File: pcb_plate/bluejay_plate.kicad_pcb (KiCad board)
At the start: 2 copper layers, 147.1 x 138.9 mm, 33 parts

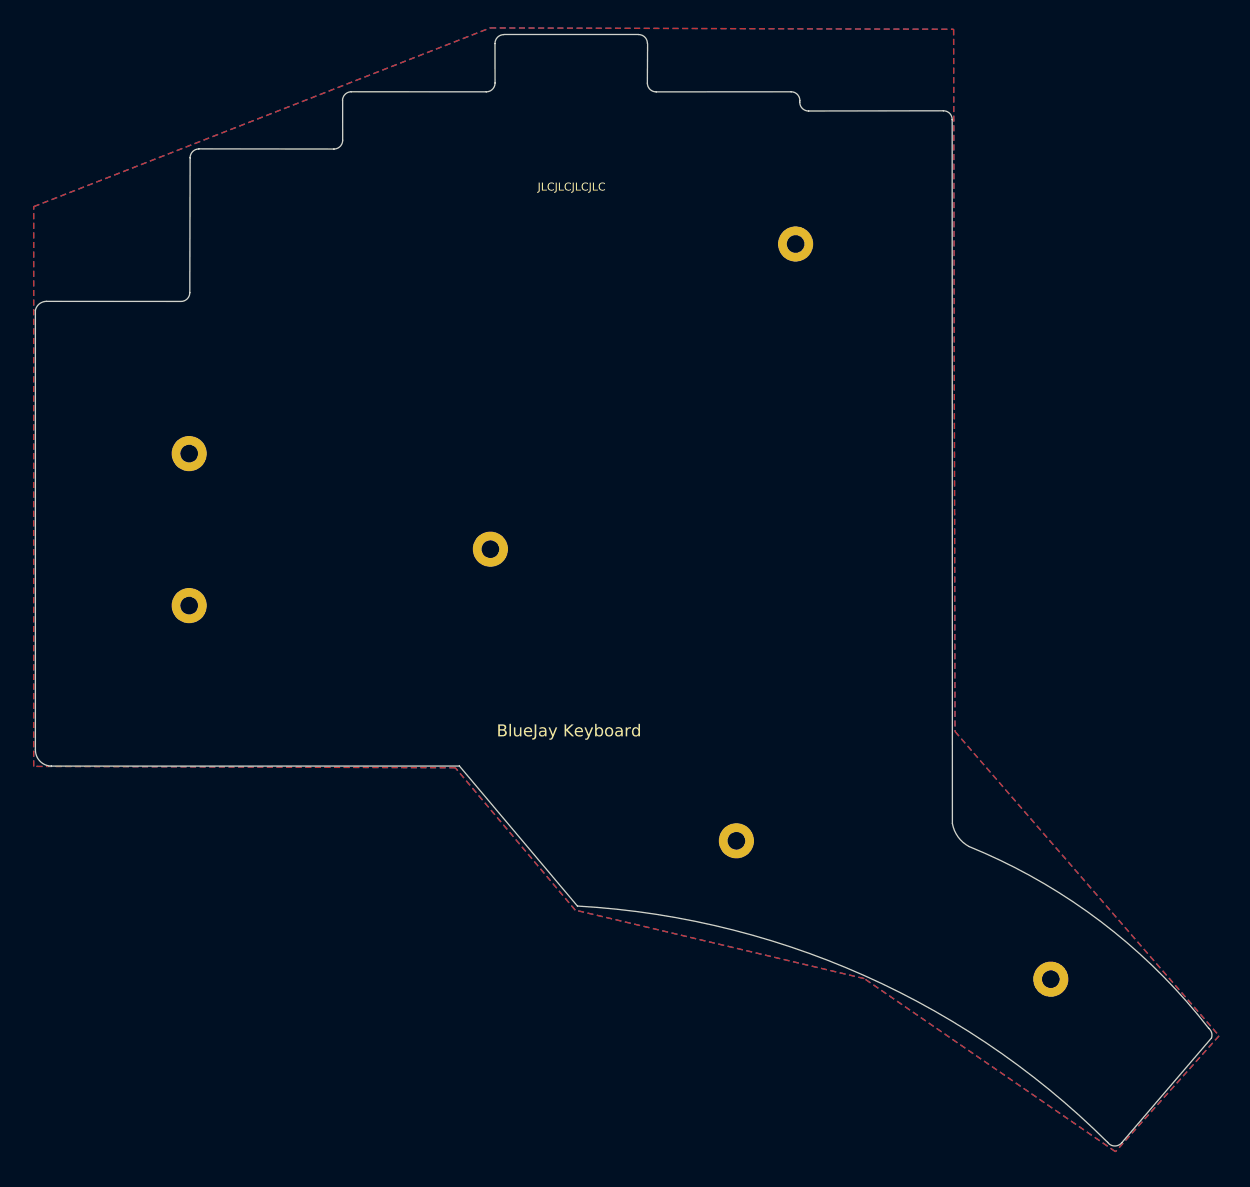
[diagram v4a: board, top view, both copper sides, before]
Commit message: Round edges of PCB
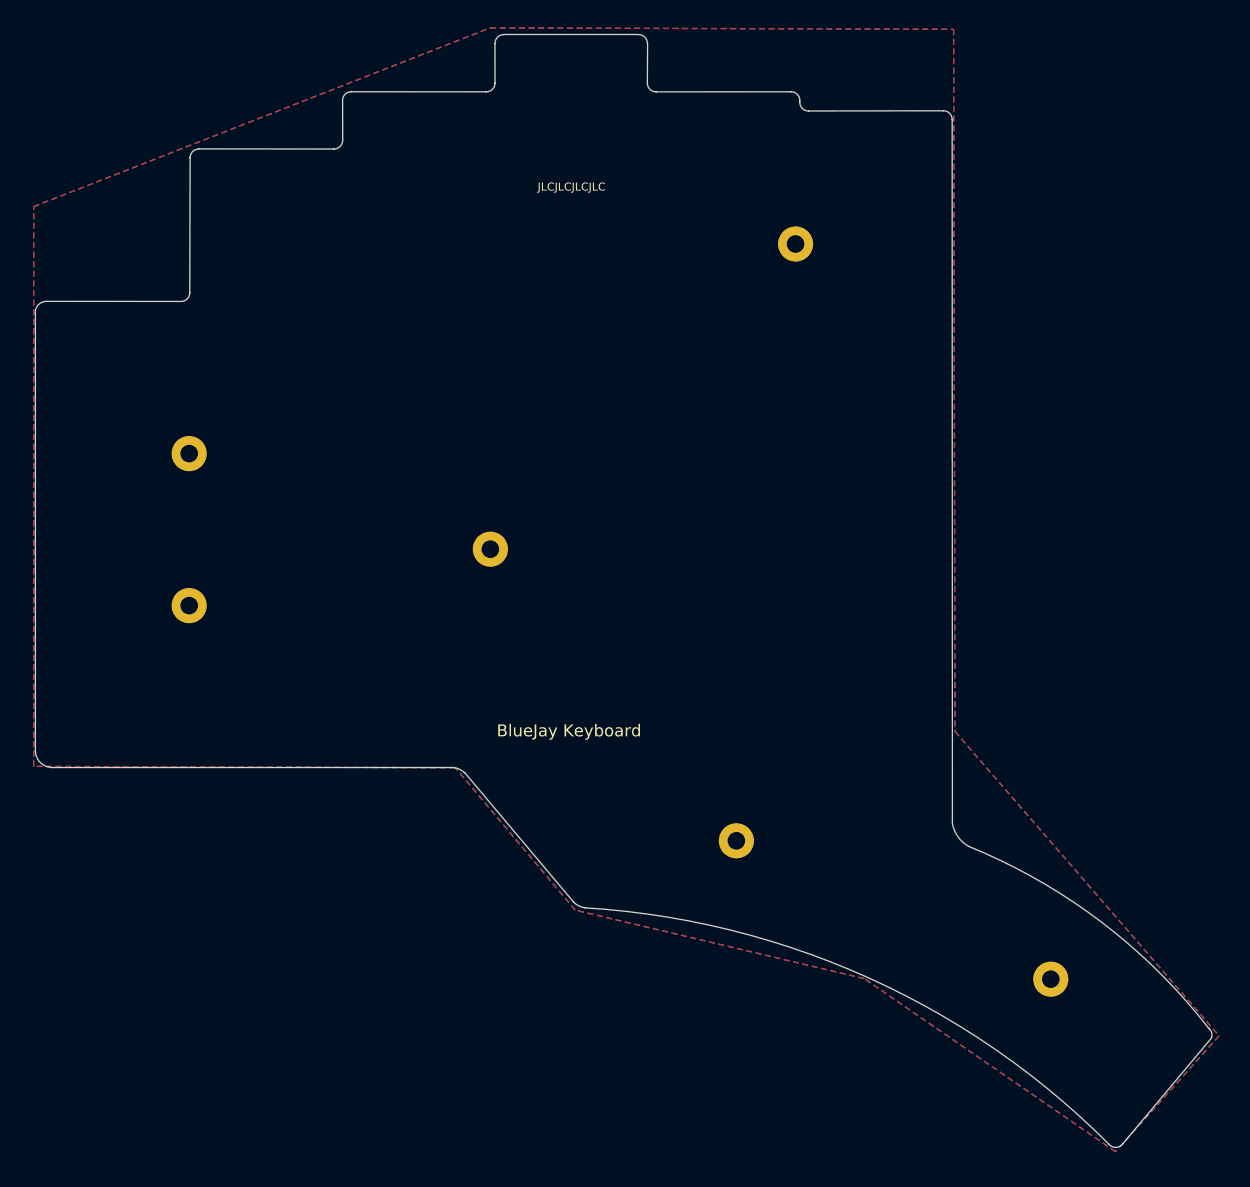
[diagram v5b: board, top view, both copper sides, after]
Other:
- board size 147.1 x 138.9 mm -> 147.1 x 139.1 mm
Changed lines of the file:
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@@
   (gr_line (start 10.630746 -45.224889) (end 27.48 -45.25) (layer "Edge.Cuts") (width 0.1))
   (gr_line (start -84.655111 -21.429254) (end -67.814889 -21.420746) (layer "Edge.Cuts") (width 0.1))
-  (gr_line (start 60.9812 70.6563) (end 49.7812 83.7263) (layer "Edge.Cuts") (width 0.1))
+  (gr_line (start 60.987489 70.653008) (end 49.88 83.9) (layer "Edge.Cuts") (width 0.1))
   (gr_line (start -47.62 -46.519254) (end -47.614889 -41.580746) (layer "Edge.Cuts") (width 0.1))
   (gr_arc (start -10.620197 -54.774034) (mid -9.84 -54.45) (end -9.530197 -53.664034) (layer "Edge.Cuts") (width 0.1))
@@
   (gr_line (start -10.620197 -54.79) (end -27.485111 -54.79) (layer "Edge.Cuts") (width 0.1))
   (gr_line (start -65.595111 -40.49) (end -48.704889 -40.470746) (layer "Edge.Cuts") (width 0.1))
+  (gr_arc (start -17.32 54.38) (mid -18.079496 54.13977) (end -18.73 53.68) (layer "Edge.Cuts") (width 0.1))
   (gr_line (start -46.56 -47.629254) (end -29.66 -47.62) (layer "Edge.Cuts") (width 0.1))
   (gr_line (start 9.52845 -46.515422) (end 9.520746 -46.314889) (layer "Edge.Cuts") (width 0.1))
   (gr_line (start -9.5 -53.664034) (end -9.529254 -48.704889) (layer "Edge.Cuts") (width 0.1))
-  (gr_arc (start -18.2688 54.1563) (mid 17.583107 62.841492) (end 48.0112 83.6963) (layer "Edge.Cuts") (width 0.1))
+  (gr_arc (start -17.32 54.38) (mid 18.101214 63.120674) (end 48.11 83.87) (layer "Edge.Cuts") (width 0.1))
   (gr_line (start 28.57 -44.15) (end 28.6 43.85) (layer "Edge.Cuts") (width 0.1))
   (gr_arc (start 60.64 69.44) (mid 61.003391 69.992176) (end 60.987489 70.653008) (layer "Edge.Cuts") (width 0.1))
   (gr_arc (start 27.48 -45.25) (mid 28.26155 -44.924578) (end 28.57 -44.14) (layer "Edge.Cuts") (width 0.1))
-  (gr_arc (start -84.02552 36.663017) (mid -85.443204 36.061839) (end -86.025519 34.6363) (layer "Edge.Cuts") (width 0.1))
-  (gr_line (start -86.024883 -20.32) (end -86.025519 34.6363) (layer "Edge.Cuts") (width 0.1))
+  (gr_arc (start -83.93 36.84) (mid -85.382325 36.242623) (end -86.025519 34.81) (layer "Edge.Cuts") (width 0.1))
+  (gr_line (start -86.024883 -20.32) (end -86.025519 34.81) (layer "Edge.Cuts") (width 0.1))
   (gr_line (start -66.685111 -39.4) (end -66.724889 -22.52) (layer "Edge.Cuts") (width 0.1))
-  (gr_line (start -84.02552 36.663017) (end -33.0188 36.6563) (layer "Edge.Cuts") (width 0.1))
+  (gr_line (start -83.93 36.84) (end -33.72 36.84) (layer "Edge.Cuts") (width 0.1))
   (gr_arc (start 10.630746 -45.224889) (mid 9.85 -45.54) (end 9.520746 -46.314889) (layer "Edge.Cuts") (width 0.1))
   (gr_arc (start -8.419254 -47.614889) (mid -9.2 -47.93) (end -9.529254 -48.704889) (layer "Edge.Cuts") (width 0.1))
   (gr_arc (start -47.614889 -41.580746) (mid -47.93 -40.8) (end -48.704889 -40.470746) (layer "Edge.Cuts") (width 0.1))
-  (gr_line (start -33.0188 36.6563) (end -18.2688 54.1563) (layer "Edge.Cuts") (width 0.1))
+  (gr_line (start -32.31 37.54) (end -18.73 53.68) (layer "Edge.Cuts") (width 0.1))
   (gr_arc (start 30.69 46.72) (mid 47.162468 56.106012) (end 60.64 69.44) (layer "Edge.Cuts") (width 0.1))
   (gr_line (start -8.419254 -47.614889) (end 8.45 -47.625422) (layer "Edge.Cuts") (width 0.1))
+  (gr_arc (start -33.72 36.84) (mid -32.960504 37.08023) (end -32.31 37.54) (layer "Edge.Cuts") (width 0.1))
   (gr_arc (start -66.724889 -22.530746) (mid -67.04 -21.75) (end -67.814889 -21.420746) (layer "Edge.Cuts") (width 0.1))
   (gr_arc (start -28.57 -48.73) (mid -28.885111 -47.949254) (end -29.66 -47.62) (layer "Edge.Cuts") (width 0.1))
   (gr_arc (start 30.69 46.72) (mid 29.316945 45.522681) (end 28.6 43.85) (layer "Edge.Cuts") (width 0.1))
   (gr_arc (start -28.575111 -53.659254) (mid -28.26 -54.44) (end -27.485111 -54.769254) (layer "Edge.Cuts") (width 0.1))
-  (gr_arc (start 49.7812 83.7263) (mid 48.888799 84.147698) (end 48.0112 83.6963) (layer "Edge.Cuts") (width 0.1))
+  (gr_arc (start 49.88 83.9) (mid 48.987603 84.321434) (end 48.11 83.87) (layer "Edge.Cuts") (width 0.1))
   (gr_arc (start -66.685111 -39.369254) (mid -66.37 -40.15) (end -65.595111 -40.479254) (layer "Edge.Cuts") (width 0.1))
   (gr_arc (start 8.43845 -47.625422) (mid 9.218647 -47.301388) (end 9.52845 -46.515422) (layer "Edge.Cuts") (width 0.1))

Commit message: Fine tuning of edge cut for plate
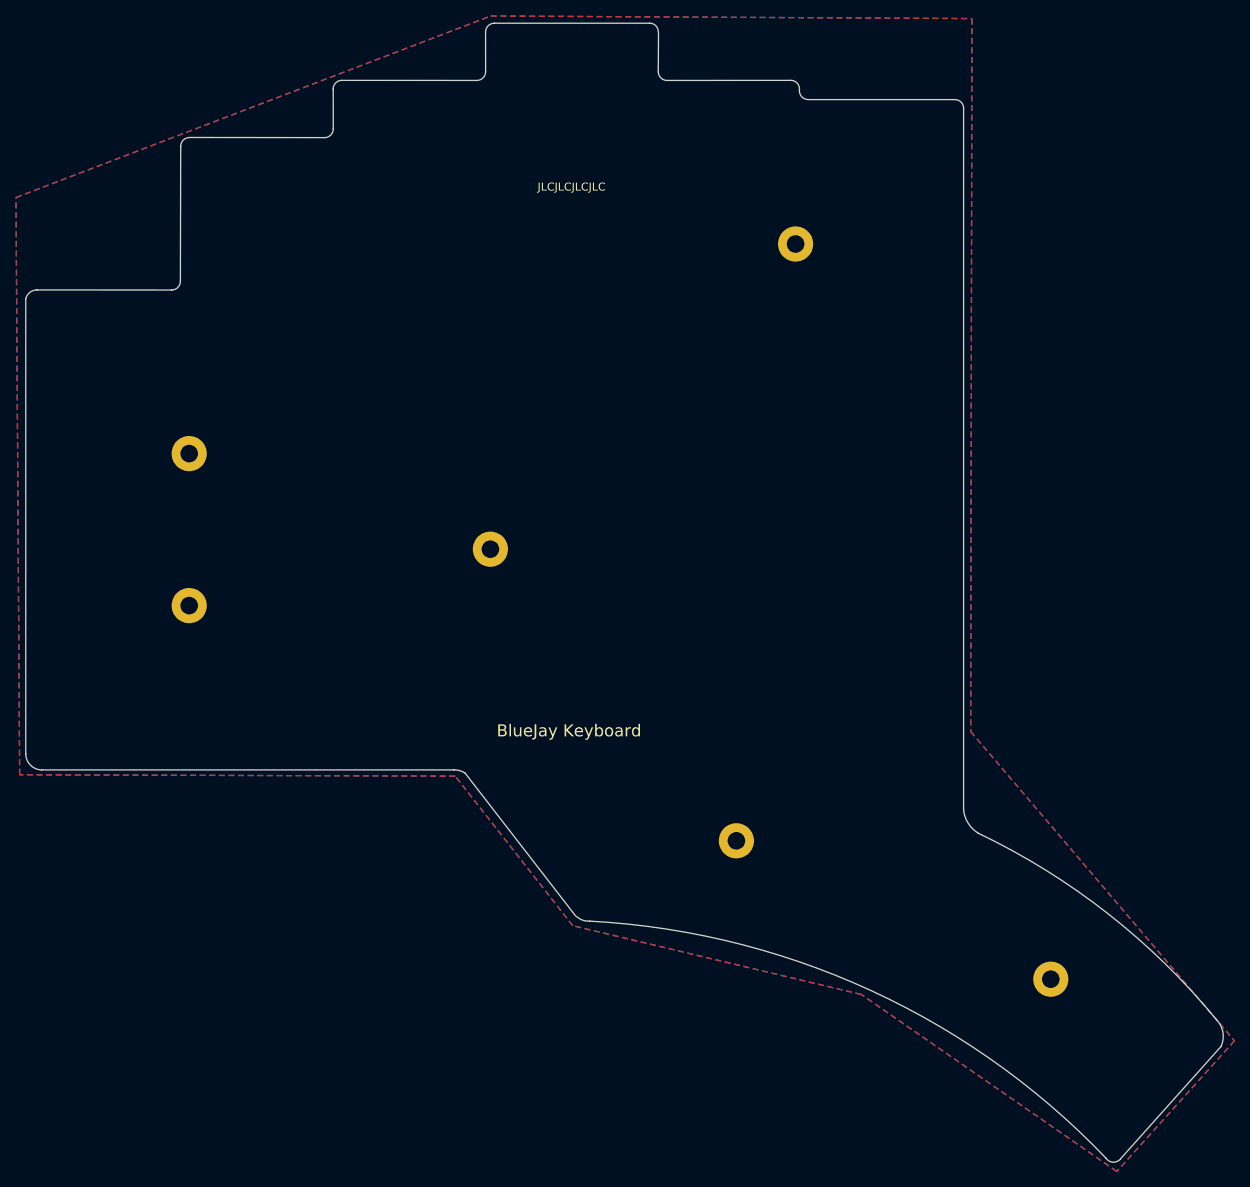
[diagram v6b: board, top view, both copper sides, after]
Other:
- board size 147.1 x 139.1 mm -> 149.7 x 142.4 mm
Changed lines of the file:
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@@
   (gr_line locked (start 26.028999 -42.674998) (end 26.028999 -42.674998) (layer "Eco1.User") (width 0.188976))
   (gr_line locked (start -16.546013 52.286989) (end -16.546013 38.286989) (layer "Eco1.User") (width 0.188976))
-  (gr_arc (start -47.635111 -46.519254) (mid -47.32 -47.3) (end -46.545111 -47.629254) (layer "Edge.Cuts") (width 0.1))
-  (gr_arc (start -86.024883 -20.32) (mid -85.533559 -21.113649) (end -84.655111 -21.429254) (layer "Edge.Cuts") (width 0.1))
-  (gr_line (start 10.630746 -45.224889) (end 27.48 -45.25) (layer "Edge.Cuts") (width 0.1))
-  (gr_line (start -84.655111 -21.429254) (end -67.814889 -21.420746) (layer "Edge.Cuts") (width 0.1))
-  (gr_line (start 60.987489 70.653008) (end 49.88 83.9) (layer "Edge.Cuts") (width 0.1))
-  (gr_line (start -47.62 -46.519254) (end -47.614889 -41.580746) (layer "Edge.Cuts") (width 0.1))
-  (gr_arc (start -10.620197 -54.774034) (mid -9.84 -54.45) (end -9.530197 -53.664034) (layer "Edge.Cuts") (width 0.1))
-  (gr_line (start -28.575111 -53.659254) (end -28.57 -48.73) (layer "Edge.Cuts") (width 0.1))
-  (gr_line (start -10.620197 -54.79) (end -27.485111 -54.79) (layer "Edge.Cuts") (width 0.1))
-  (gr_line (start -65.595111 -40.49) (end -48.704889 -40.470746) (layer "Edge.Cuts") (width 0.1))
-  (gr_arc (start -17.32 54.38) (mid -18.079496 54.13977) (end -18.73 53.68) (layer "Edge.Cuts") (width 0.1))
-  (gr_line (start -46.56 -47.629254) (end -29.66 -47.62) (layer "Edge.Cuts") (width 0.1))
-  (gr_line (start 9.52845 -46.515422) (end 9.520746 -46.314889) (layer "Edge.Cuts") (width 0.1))
-  (gr_line (start -9.5 -53.664034) (end -9.529254 -48.704889) (layer "Edge.Cuts") (width 0.1))
-  (gr_arc (start -17.32 54.38) (mid 18.101214 63.120674) (end 48.11 83.87) (layer "Edge.Cuts") (width 0.1))
-  (gr_line (start 28.57 -44.15) (end 28.6 43.85) (layer "Edge.Cuts") (width 0.1))
-  (gr_arc (start 60.64 69.44) (mid 61.003391 69.992176) (end 60.987489 70.653008) (layer "Edge.Cuts") (width 0.1))
-  (gr_arc (start 27.48 -45.25) (mid 28.26155 -44.924578) (end 28.57 -44.14) (layer "Edge.Cuts") (width 0.1))
-  (gr_arc (start -83.93 36.84) (mid -85.382325 36.242623) (end -86.025519 34.81) (layer "Edge.Cuts") (width 0.1))
-  (gr_line (start -86.024883 -20.32) (end -86.025519 34.81) (layer "Edge.Cuts") (width 0.1))
-  (gr_line (start -66.685111 -39.4) (end -66.724889 -22.52) (layer "Edge.Cuts") (width 0.1))
-  (gr_line (start -83.93 36.84) (end -33.72 36.84) (layer "Edge.Cuts") (width 0.1))
-  (gr_arc (start 10.630746 -45.224889) (mid 9.85 -45.54) (end 9.520746 -46.314889) (layer "Edge.Cuts") (width 0.1))
-  (gr_arc (start -8.419254 -47.614889) (mid -9.2 -47.93) (end -9.529254 -48.704889) (layer "Edge.Cuts") (width 0.1))
-  (gr_arc (start -47.614889 -41.580746) (mid -47.93 -40.8) (end -48.704889 -40.470746) (layer "Edge.Cuts") (width 0.1))
-  (gr_line (start -32.31 37.54) (end -18.73 53.68) (layer "Edge.Cuts") (width 0.1))
-  (gr_arc (start 30.69 46.72) (mid 47.162468 56.106012) (end 60.64 69.44) (layer "Edge.Cuts") (width 0.1))
-  (gr_line (start -8.419254 -47.614889) (end 8.45 -47.625422) (layer "Edge.Cuts") (width 0.1))
-  (gr_arc (start -33.72 36.84) (mid -32.960504 37.08023) (end -32.31 37.54) (layer "Edge.Cuts") (width 0.1))
-  (gr_arc (start -66.724889 -22.530746) (mid -67.04 -21.75) (end -67.814889 -21.420746) (layer "Edge.Cuts") (width 0.1))
-  (gr_arc (start -28.57 -48.73) (mid -28.885111 -47.949254) (end -29.66 -47.62) (layer "Edge.Cuts") (width 0.1))
-  (gr_arc (start 30.69 46.72) (mid 29.316945 45.522681) (end 28.6 43.85) (layer "Edge.Cuts") (width 0.1))
-  (gr_arc (start -28.575111 -53.659254) (mid -28.26 -54.44) (end -27.485111 -54.769254) (layer "Edge.Cuts") (width 0.1))
-  (gr_arc (start 49.88 83.9) (mid 48.987603 84.321434) (end 48.11 83.87) (layer "Edge.Cuts") (width 0.1))
-  (gr_arc (start -66.685111 -39.369254) (mid -66.37 -40.15) (end -65.595111 -40.479254) (layer "Edge.Cuts") (width 0.1))
-  (gr_arc (start 8.43845 -47.625422) (mid 9.218647 -47.301388) (end 9.52845 -46.515422) (layer "Edge.Cuts") (width 0.1))
+  (gr_arc (start -48.811552 -47.945605) (mid -48.496441 -48.726351) (end -47.721552 -49.055605) (layer "Edge.Cuts") (width 0.1))
+  (gr_arc (start -87.23 -21.74) (mid -86.725569 -22.541982) (end -85.831552 -22.855605) (layer "Edge.Cuts") (width 0.1))
+  (gr_line (start 10.630746 -46.65) (end 28.91 -46.65) (layer "Edge.Cuts") (width 0.1))
+  (gr_line (start -85.831552 -22.855605) (end -68.99133 -22.847097) (layer "Edge.Cuts") (width 0.1))
+  (gr_line (start 62.17 71.72) (end 49.62 85.75) (layer "Edge.Cuts") (width 0.1))
+  (gr_line (start -48.796441 -47.945605) (end -48.79133 -43.007097) (layer "Edge.Cuts") (width 0.1))
+  (gr_arc (start -9.25557 -56.203879) (mid -8.47537 -55.879841) (end -8.16557 -55.093879) (layer "Edge.Cuts") (width 0.1))
+  (gr_line (start -29.751552 -55.085605) (end -29.746441 -50.156351) (layer "Edge.Cuts") (width 0.1))
+  (gr_line (start -9.26 -56.2) (end -28.66 -56.2) (layer "Edge.Cuts") (width 0.1))
+  (gr_line (start -66.771552 -41.916351) (end -49.88133 -41.897097) (layer "Edge.Cuts") (width 0.1))
+  (gr_arc (start -16.74 56.04) (mid -17.619397 55.917949) (end -18.38 55.46) (layer "Edge.Cuts") (width 0.1))
+  (gr_line (start -47.736441 -49.055605) (end -30.836441 -49.046351) (layer "Edge.Cuts") (width 0.1))
+  (gr_line (start 9.483077 -47.945267) (end 9.475373 -47.744734) (layer "Edge.Cuts") (width 0.1))
+  (gr_line (start -8.135373 -55.093879) (end -8.164627 -50.134734) (layer "Edge.Cuts") (width 0.1))
+  (gr_arc (start -16.74 56.04) (mid 18.380681 64.696706) (end 47.83 85.7) (layer "Edge.Cuts") (width 0.1))
+  (gr_line (start 30 -45.54) (end 30 42.15) (layer "Edge.Cuts") (width 0.1))
+  (gr_arc (start 61.62 68.37) (mid 62.419111 69.958952) (end 62.17 71.72) (layer "Edge.Cuts") (width 0.1))
+  (gr_arc (start 28.91 -46.65) (mid 29.690197 -46.325966) (end 30 -45.54) (layer "Edge.Cuts") (width 0.1))
+  (gr_arc (start -85.23 37.14) (mid -86.648353 36.53717) (end -87.23 35.11) (layer "Edge.Cuts") (width 0.1))
+  (gr_line (start -87.23 -21.74) (end -87.23 35.11) (layer "Edge.Cuts") (width 0.1))
+  (gr_line (start -67.861552 -40.826351) (end -67.90133 -23.946351) (layer "Edge.Cuts") (width 0.1))
+  (gr_line (start -85.23 37.14) (end -33.72 37.14) (layer "Edge.Cuts") (width 0.1))
+  (gr_arc (start 10.585373 -46.654734) (mid 9.804629 -46.969847) (end 9.475373 -47.744734) (layer "Edge.Cuts") (width 0.1))
+  (gr_arc (start -7.054627 -49.044734) (mid -7.835373 -49.359845) (end -8.164627 -50.134734) (layer "Edge.Cuts") (width 0.1))
+  (gr_arc (start -48.79133 -43.007097) (mid -49.106441 -42.226351) (end -49.88133 -41.897097) (layer "Edge.Cuts") (width 0.1))
+  (gr_line (start -32.31 37.54) (end -18.47 55.43) (layer "Edge.Cuts") (width 0.1))
+  (gr_arc (start 31.81 45.04) (mid 47.995192 55.066627) (end 61.62 68.37) (layer "Edge.Cuts") (width 0.1))
+  (gr_line (start -7.05 -49.044734) (end 8.404627 -49.055267) (layer "Edge.Cuts") (width 0.1))
+  (gr_arc (start -33.72 37.14) (mid -32.98386 37.23023) (end -32.31 37.54) (layer "Edge.Cuts") (width 0.1))
+  (gr_arc (start -67.90133 -23.957097) (mid -68.216441 -23.176351) (end -68.99133 -22.847097) (layer "Edge.Cuts") (width 0.1))
+  (gr_arc (start -29.746441 -50.156351) (mid -30.061552 -49.375605) (end -30.836441 -49.046351) (layer "Edge.Cuts") (width 0.1))
+  (gr_arc (start 31.782503 45.016513) (mid 30.564308 43.786562) (end 30 42.15) (layer "Edge.Cuts") (width 0.1))
+  (gr_arc (start -29.751552 -55.085605) (mid -29.436575 -55.86887) (end -28.66 -56.2) (layer "Edge.Cuts") (width 0.1))
+  (gr_arc (start 49.59 85.78) (mid 48.690274 86.173968) (end 47.83 85.7) (layer "Edge.Cuts") (width 0.1))
+  (gr_arc (start -67.861552 -40.795605) (mid -67.546441 -41.576351) (end -66.771552 -41.905605) (layer "Edge.Cuts") (width 0.1))
+  (gr_arc (start 8.393077 -49.055267) (mid 9.173279 -48.731231) (end 9.483077 -47.945267) (layer "Edge.Cuts") (width 0.1))
   (gr_text "JLCJLCJLCJLC" (at -19 -35.74) (layer "F.SilkS")
     (effects (font (size 1 1) (thickness 0.15)))
@@
     (polygon
       (pts
-        (xy -29.18 -55.61)
-        (xy 28.75 -55.44)
-        (xy 28.93 32.34)
-        (xy 61.936763 70.377262)
-        (xy 48.99 84.86)
-        (xy 17.58 63.22)
-        (xy -18.54 54.67)
-        (xy -33.54 36.87)
-        (xy -86.24 36.7)
-        (xy -86.24 -33.27)
+        (xy -29.1 -57.1)
+        (xy 31.04249 -56.775717)
+        (xy 30.885683 32.343488)
+        (xy 63.86 71)
+        (xy 49.15 87.33)
+        (xy 17.205584 65.204371)
+        (xy -18.854416 56.614371)
+        (xy -33.543275 37.918616)
+        (xy -87.993275 37.748616)
+        (xy -88.449914 -34.412332)
       )
     )
